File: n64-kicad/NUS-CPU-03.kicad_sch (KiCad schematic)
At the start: 14 parts, among them P1 Expansion Pak Connector, U11 RDRAM18-NUS, U14 RDRAM18-NUS, U8 CPU-NUS

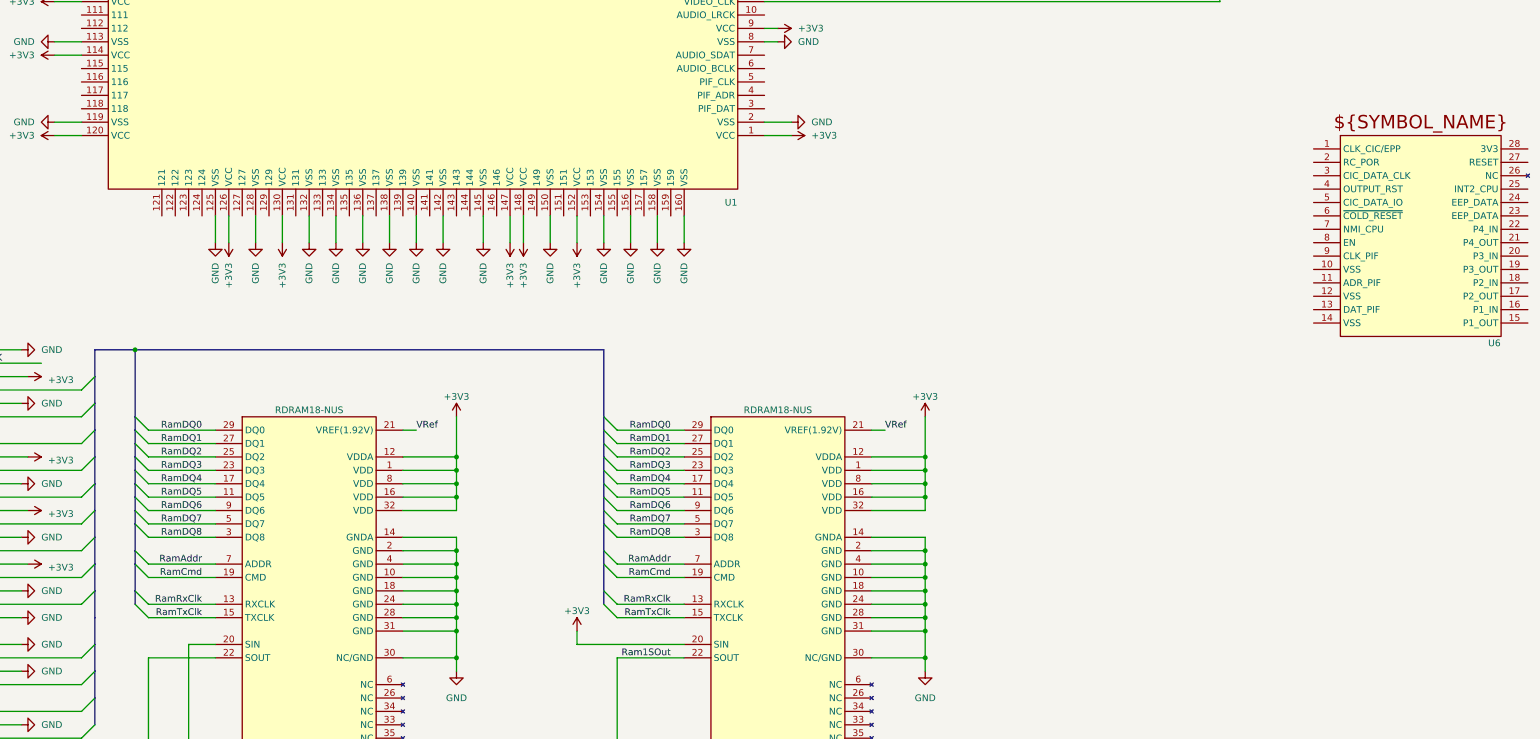
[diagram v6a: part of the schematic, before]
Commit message: Fix labels and update PDF
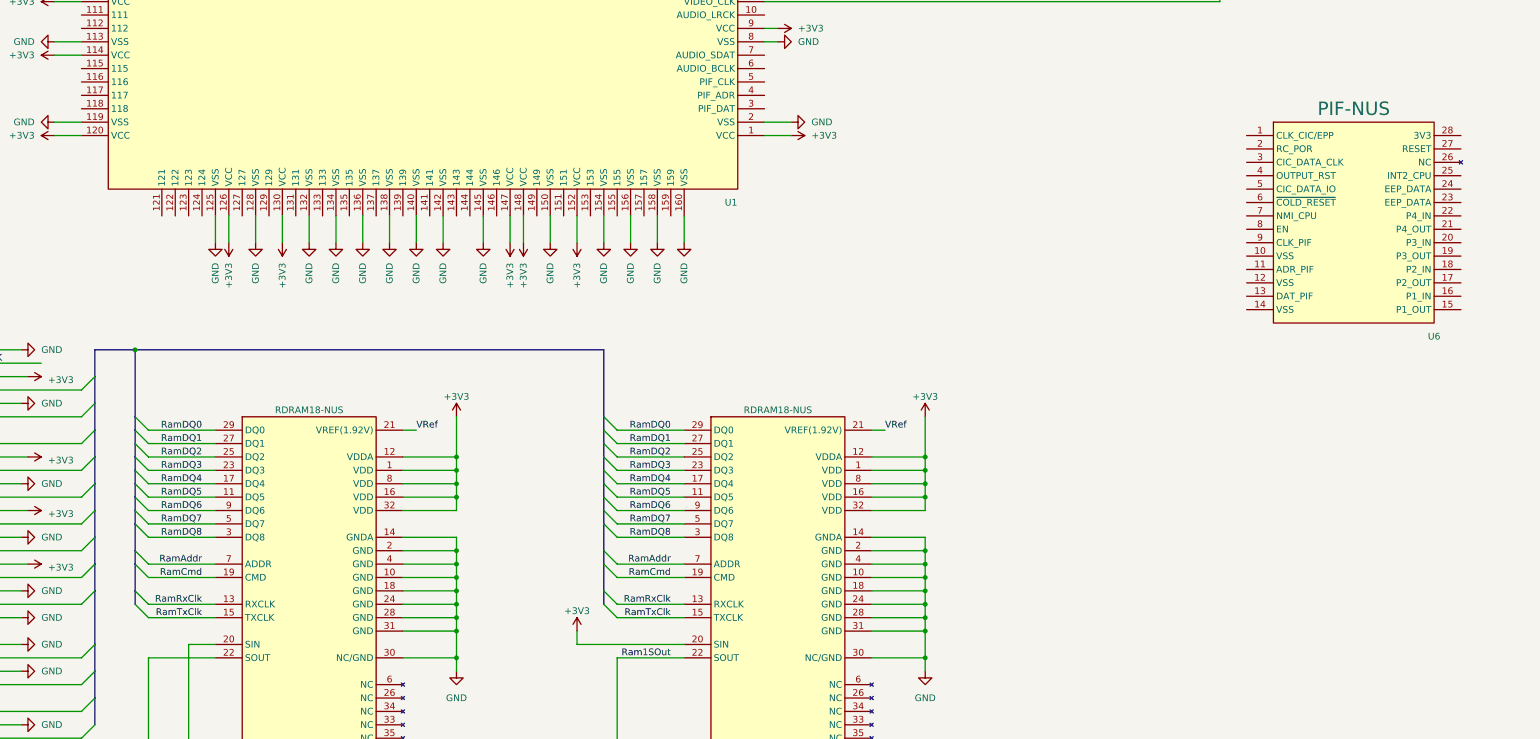
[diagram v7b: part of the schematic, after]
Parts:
- U6: value ~ -> PIF-NUS
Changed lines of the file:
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@@
     (stroke (width 0) (type default))
   )
-  (bus (pts (xy 299.72 269.24) (xy 299.72 264.16))
+  (bus (pts (xy 299.72 264.16) (xy 299.72 274.32))
     (stroke (width 0) (type default))
   )
@@
   )
   (wire (pts (xy 406.4 193.04) (xy 406.4 198.12))
-    (stroke (width 0) (type default))
-  )
-  (bus (pts (xy 299.72 274.32) (xy 299.72 269.24))
     (stroke (width 0) (type default))
   )
@@
         (path "/62362fc5-d8b0-453c-8cf3-9bf5adb1c5ec/fe0f5ce9-be45-40ad-8b42-2b325418535e"
           (reference "#PWR069") (unit 1)
-        )
-      )
-    )
-  )
-  (symbol (lib_id "n64:PIF-NUS") (at 566.42 218.44 0) (unit 1)
-    (in_bom yes) (on_board yes) (dnp no)
-    (property "Reference" "U6" (at 565.15 217.17 0)
-      (effects (font (size 1.27 1.27)))
-    )
-    (property "Value" "~" (at 566.42 218.44 0)
-      (effects (font (size 1.27 1.27)))
-    )
-    (property "Footprint" "" (at 566.42 218.44 0)
-      (effects (font (size 1.27 1.27)) hide)
-    )
-    (property "Datasheet" "" (at 566.42 218.44 0)
-      (effects (font (size 1.27 1.27)) hide)
-    )
-    (pin "1")
-    (pin "10")
-    (pin "11")
-    (pin "12")
-    (pin "13")
-    (pin "14")
-    (pin "15")
-    (pin "16")
-    (pin "17")
-    (pin "18")
-    (pin "19")
-    (pin "2")
-    (pin "20")
-    (pin "21")
-    (pin "22")
-    (pin "23")
-    (pin "24")
-    (pin "25")
-    (pin "26")
-    (pin "27")
-    (pin "28")
-    (pin "3")
-    (pin "4")
-    (pin "5")
-    (pin "6")
-    (pin "7")
-    (pin "8")
-    (pin "9")
-    (instances
-      (project "n64-kicad"
-        (path "/62362fc5-d8b0-453c-8cf3-9bf5adb1c5ec/fe0f5ce9-be45-40ad-8b42-2b325418535e"
-          (reference "U6") (unit 1)
         )
       )
@@
         )
       )
+    )
+  )
+  (symbol (lib_id "n64:PIF-NUS") (at 553.72 215.9 0) (unit 1)
+    (in_bom yes) (on_board yes) (dnp no) (fields_autoplaced)
+    (property "Reference" "U6" (at 553.72 215.9 0) (do_not_autoplace)
+      (effects (font (size 1.27 1.27)))
+    )
+    (property "Value" "PIF-NUS" (at 538.48 172.72 0) (do_not_autoplace)
+      (effects (font (size 2.54 2.54)))
+    )
+    (property "Footprint" "" (at 553.72 215.9 0)
+      (effects (font (size 1.27 1.27)) hide)
+    )
+    (property "Datasheet" "" (at 553.72 215.9 0)
+      (effects (font (size 1.27 1.27)) hide)
+    )
+    (pin "1")
+    (pin "10")
+    (pin "11")
+    (pin "12")
+    (pin "13")
+    (pin "14")
+    (pin "15")
+    (pin "16")
+    (pin "17")
+    (pin "18")
+    (pin "19")
+    (pin "2")
+    (pin "20")
+    (pin "21")
+    (pin "22")
+    (pin "23")
+    (pin "24")
+    (pin "25")
+    (pin "26")
+    (pin "27")
+    (pin "28")
+    (pin "3")
+    (pin "4")
+    (pin "5")
+    (pin "6")
+    (pin "7")
+    (pin "8")
+    (pin "9")
+    (instances
+      (project "n64-kicad"
+        (path "/62362fc5-d8b0-453c-8cf3-9bf5adb1c5ec/fe0f5ce9-be45-40ad-8b42-2b325418535e"
+          (reference "U6") (unit 1)
+        )
+      )
